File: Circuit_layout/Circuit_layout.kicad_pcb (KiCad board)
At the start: 2 copper layers, 177.8 x 127 mm, 188 parts, among them CON1 AVR-JTAG-10, J1 Spare_Conns, J4 Motor_Ctrl, J5 RJ12, P1 TSV, P2 CONN_02X10, P3 CONN_02X07, Q1 ZVP4525G, Q2 MMBF170, Q3 MMBF170, SW1 SW_PUSH, SW2 TS5A3159-Q1, SW3 JS202011CQN, U1 PDM2-S24-S12, U10 MCP2551-I/SN, U11 TLP293, U12 TLP293, U13 PDQ10-D, U16 LTC3638, U17 MCP6004, U18 TS912, U19 ACPL-C870, U2 MCP6002, U20 ACPL-C870, U21 MCP6001, U22 TS372, U23 TLP293, U24 TLP293, U3 MCP6004, U4 LM95071-Q1, U5 LM7810CT, U6 TS912, U7 AT90CAN128-A, U8 74ACT11030, U9 TLP293, Y1 10MHz

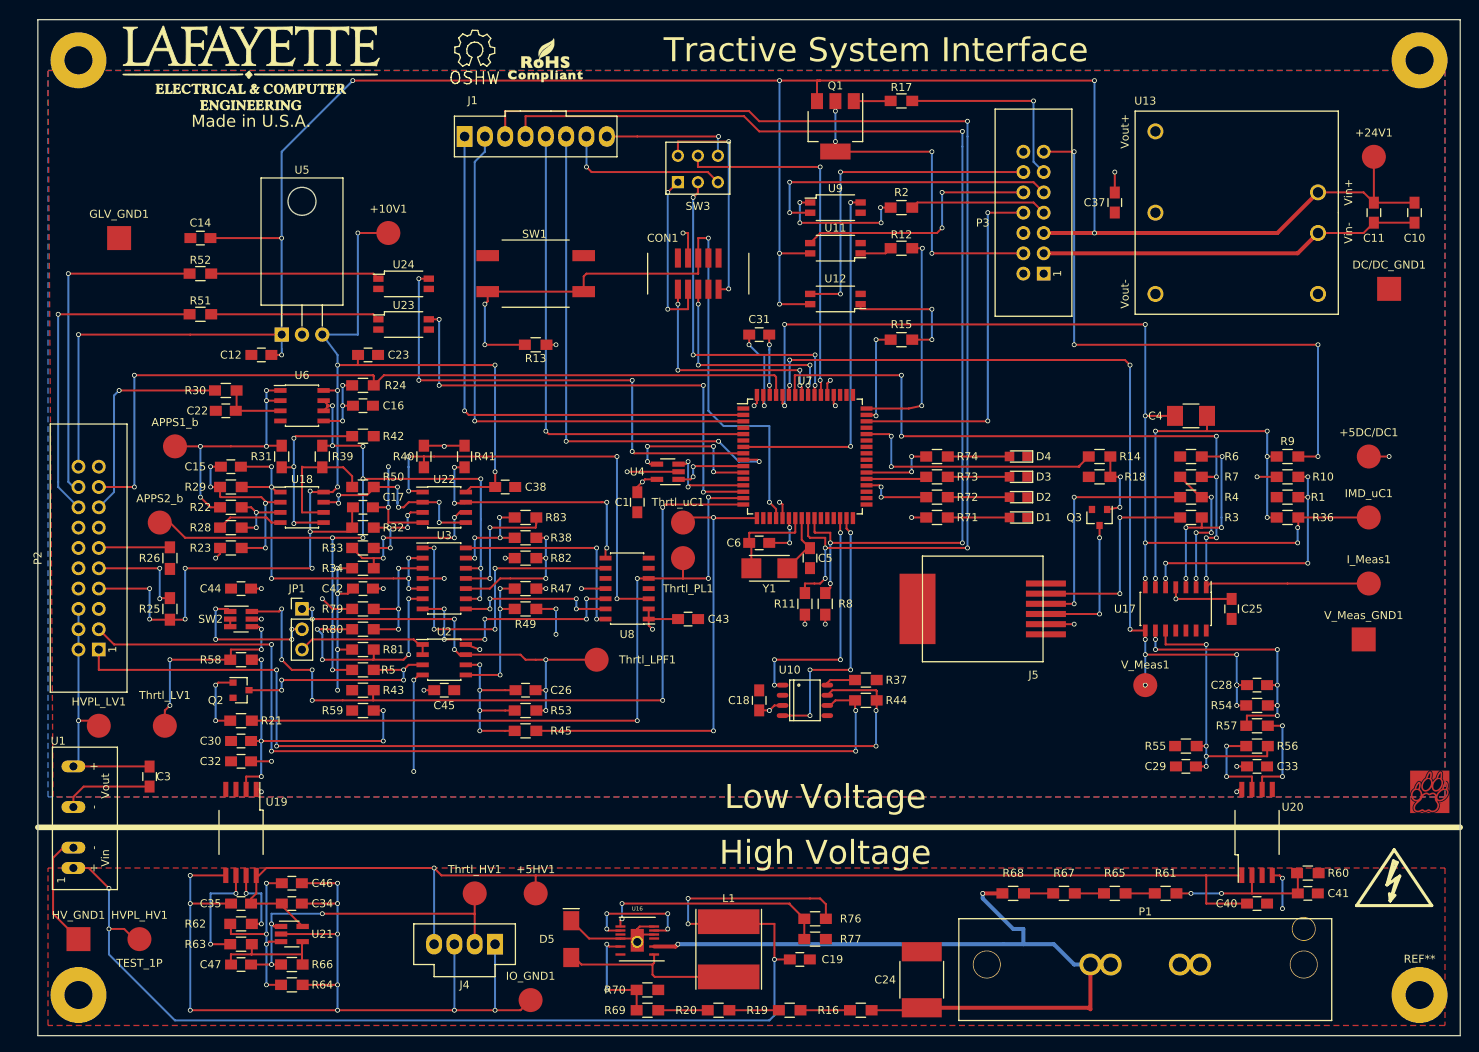
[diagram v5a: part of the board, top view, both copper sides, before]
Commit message: fixed changes proposed by prof. nadovich.
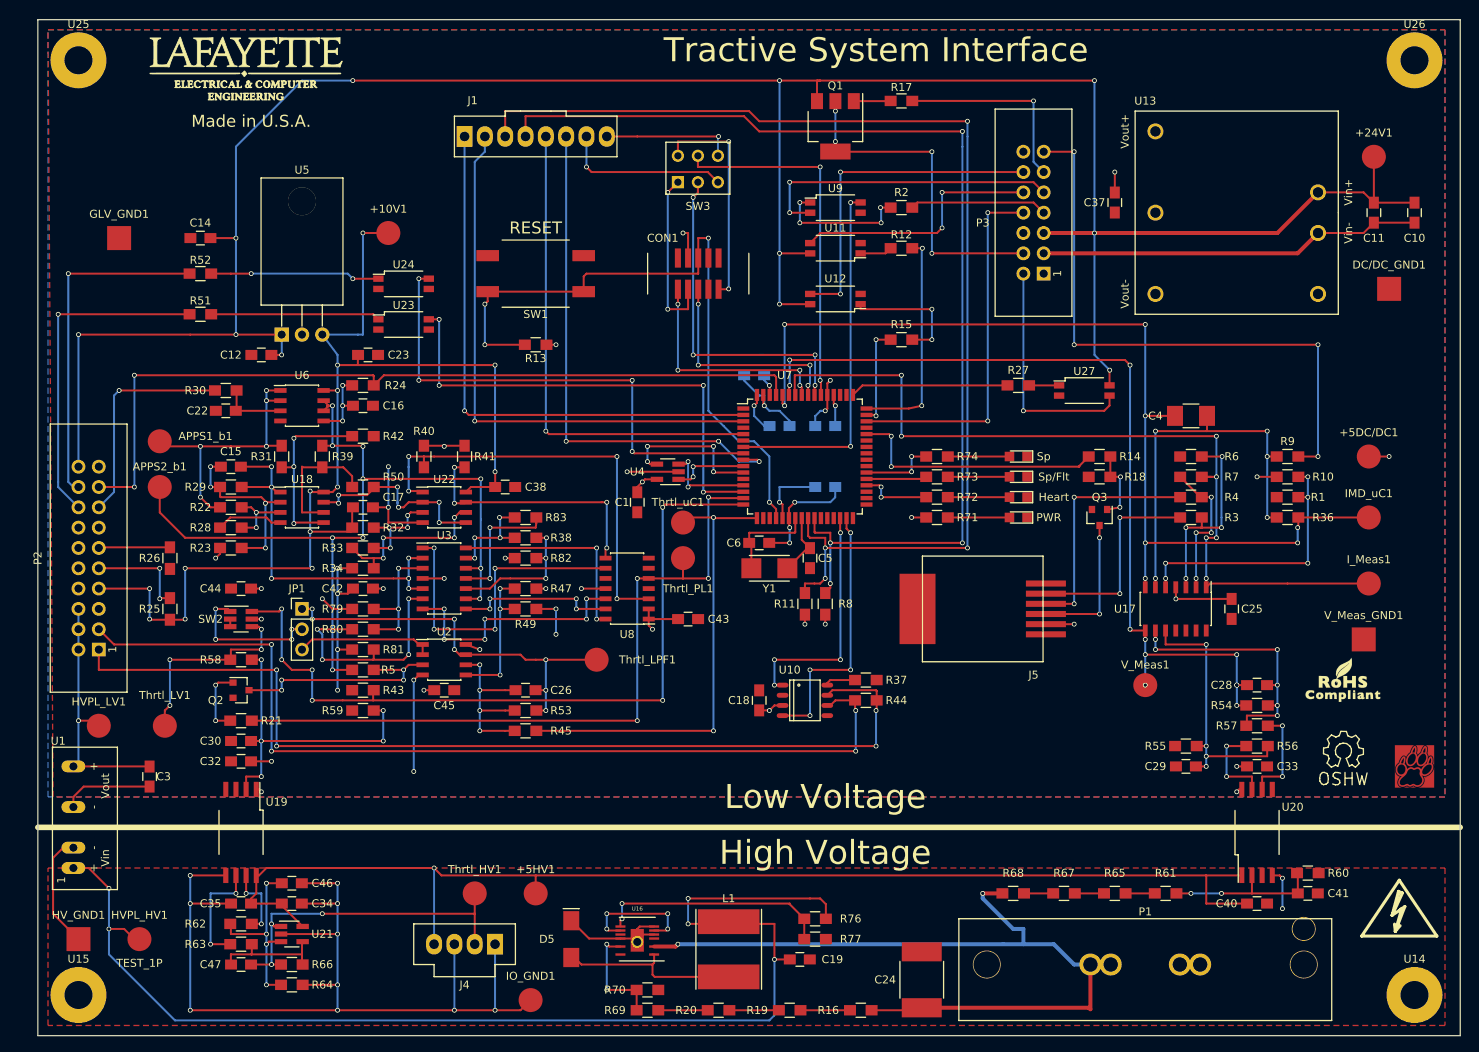
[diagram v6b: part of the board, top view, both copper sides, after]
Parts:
- removed the ? at (35.6, 34.3)
- removed the ? at (203.2, 34.3)
- removed the ? at (35.6, 151.1)
- removed APPS1_b: APPS1_b, Measurement_Points:Measurement_Point_Round-SMD-Pad_Big
- removed APPS2_b: APPS2_b, Measurement_Points:Measurement_Point_Round-SMD-Pad_Big
- removed the G*** at (57.1, 35.6)
- removed the REF** at (203.2, 151.1)
- added APPS1_b1: APPS1_b, Measurement_Points:Measurement_Point_Round-SMD-Pad_Big, F.Cu at (45.7, 81.9)
- added APPS2_b1: APPS2_b, Measurement_Points:Measurement_Point_Round-SMD-Pad_Big, F.Cu at (45.7, 87.6)
- added C2: 0.1u, Capacitors_SMD:C_0805_HandSoldering, B.Cu at (128.9, 80.0)
- added C7: 0.1u, Capacitors_SMD:C_0805_HandSoldering, B.Cu at (123.2, 80.0)
- added C8: 0.1u, Capacitors_SMD:C_0805_HandSoldering, B.Cu at (128.9, 87.6)
- added G***: LOGO, custom_footprints:logo_lafayette_ece_24mmx9mm, F.Cu at (56.5, 35.6)
- added R27: 150, Resistors_SMD:R_0805_HandSoldering, F.Cu at (153.0, 74.9)
- added U14: Mounting_hole, Mounting_Holes:MountingHole_3.5mm_Pad, F.Cu at (202.6, 151.1)
- added U15: Mounting_hole, Mounting_Holes:MountingHole_3.5mm_Pad, F.Cu at (35.6, 151.1)
- added U25: Mounting_hole, Mounting_Holes:MountingHole_3.5mm_Pad, F.Cu at (35.6, 34.3)
- added U26: Mounting_hole, Mounting_Holes:MountingHole_3.5mm_Pad, F.Cu at (202.6, 34.3)
- added U27: TLP293, Housings_SSOP:SOP-4_4.4x2.8mm_Pitch1.27mm, F.Cu at (161.3, 75.6)
- C31: moved to B.Cu
- U5: footprint TO_SOT_Packages_THT:TO-220_Horizontal -> custom_footprints:TO-220_Horizontal_Plated_Hole
- moved REF** 139.5 mm to (193.7, 120.7)
- moved G*** 126.3 mm to (193.7, 111.8)
- moved C31 5.12 mm to (120.0, 73.7)
- moved ? 3.86 mm to (200.7, 141.0)
- moved ? 3.86 mm to (201.3, 141.0)
- moved VAL 3.70 mm to (202.6, 122.6)
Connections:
- P3 pad 2: CH_GND -> CC_LED
- U5 pad 0: (no net) -> CH_GND
- U7 pad 49: Net-(U7-Pad49) -> /Status Lights/CC_LED_CTRL
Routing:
- net CC_LED: track 0.00 -> 29.4 mm, vias 0 -> 1
- net +24V: track 295.2 -> 315.4 mm, vias 10 -> 12
- net /Status Lights/CC_LED_CTRL: track 0.00 -> 19.8 mm
- net CH_GND: track 115.5 -> 129.0 mm, vias 18 -> 19
- net +5V: track 78.8 -> 91.4 mm
- net Net-(C31-Pad1): track 7.57 -> 2.75 mm, vias 2 -> 1
- net Net-(R27-Pad1): track 0.00 -> 3.76 mm
- net /ThrottlePlausibility/APPS2_b: track 102.9 -> 106.6 mm
- net ~RESET_AVR: track 88.3 -> 86.1 mm
- net /ThrottlePlausibility/APPS1_b: track 33.7 -> 35.9 mm
- net (no net): track 0.02 -> 0.65 mm
- net Net-(R52-Pad2): vias 0 -> 2
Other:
- net class Default: clearance 0.254 -> 0.2032
- rule trace_clearance: 0.254 -> 0.2032
- board text added: "Heart"
- board text added: "PWR"
- board text added: "RESET"
- board text added: "Sp"
- board text added: "Sp/Flt"

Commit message: small changes
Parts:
- moved C8 3.86 mm to (125.1, 88.3)
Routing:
- net +5V: track 91.4 -> 86.6 mm
- net CH_GND: track 129.0 -> 128.9 mm, vias 19 -> 20
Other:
- board text added: "Designed by: Jack Plumb and Adam Ness"
- board text removed: "Update U5 to have horizontal footprint"
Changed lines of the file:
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@@
   (general
     (links 413)
-    (no_connects 1)
-    (area 30.404999 29.134999 208.355001 156.285001)
+    (no_connects 0)
+    (area -39.052858 17.47 231.825715 156.905)
     (thickness 1.6)
-    (drawings 18)
-    (tracks 1610)
+    (drawings 21)
+    (tracks 1612)
     (zones 0)
     (modules 193)
@@
     (41 Cmts.User user)
     (42 Eco1.User user)
-    (43 Eco2.User user)
+    (43 Eco2.User user hide)
     (44 Edge.Cuts user)
     (45 Margin user)
@@
     (mod_text_size 1 1)
     (mod_text_width 0.15)
-    (pad_size 3 3)
-    (pad_drill 0)
+    (pad_size 4.5 4.5)
+    (pad_drill 3.5)
     (pad_to_mask_clearance 0.2)
     (aux_axis_origin 0 0)
@@
   )
   (module Capacitors_SMD:C_0805_HandSoldering (layer B.Cu)
-    (at 128.905 87.63)
+    (at 125.095 88.265)
     (descr "Capacitor SMD 0805, hand soldering")
     (tags "capacitor 0805")
@@
     (descr "Mounting Hole 3.5mm")
     (tags "mounting hole 3.5mm")
-    (fp_text reference U14 (at 0 -4.5) (layer F.SilkS)
+    (fp_text reference U14 (at 0 -4.5) (layer F.SilkS) hide
       (effects (font (size 1 1) (thickness 0.15)))
     )
@@
     (descr "Mounting Hole 3.5mm")
     (tags "mounting hole 3.5mm")
-    (fp_text reference U15 (at 0 -4.5) (layer F.SilkS)
+    (fp_text reference U15 (at 0 -4.5) (layer F.SilkS) hide
       (effects (font (size 1 1) (thickness 0.15)))
     )
@@
     (descr "Mounting Hole 3.5mm")
     (tags "mounting hole 3.5mm")
-    (fp_text reference U25 (at 0 -4.5) (layer F.SilkS)
+    (fp_text reference U25 (at 0 -4.5) (layer F.SilkS) hide
       (effects (font (size 1 1) (thickness 0.15)))
     )
@@
     (descr "Mounting Hole 3.5mm")
     (tags "mounting hole 3.5mm")
-    (fp_text reference U26 (at 0 -4.5) (layer F.SilkS)
+    (fp_text reference U26 (at 0 -4.5) (layer F.SilkS) hide
       (effects (font (size 1 1) (thickness 0.15)))
     )
@@
     (fp_line (start 7.79 -19.71) (end -2.71 -19.71) (layer F.CrtYd) (width 0.05))
     (fp_circle (center 2.54 -16.66) (end 4.39 -16.66) (layer F.Fab) (width 0.1))
-    (pad 0 thru_hole circle (at 2.54 -16.66) (size 3.5 3.5) (drill 3.5) (layers *.Cu *.Mask F.SilkS)
+    (pad 0 thru_hole circle (at 2.54 -16.66) (size 4.5 4.5) (drill 3.5) (layers *.Cu *.Mask F.SilkS)
       (net 1 CH_GND))
     (pad 1 thru_hole rect (at 0 0) (size 1.8 1.8) (drill 1) (layers *.Cu *.Mask)
@@
       (xy 0.465667 0.021167)) (layer F.SilkS) (width 0.01))
   )
+  (gr_text "High Voltage" (at 128.905 133.35) (layer B.SilkS)
+    (effects (font (size 3 3) (thickness 0.3)) (justify mirror))
+  )
+  (gr_text "Low Voltage" (at 128.905 126.365) (layer B.SilkS)
+    (effects (font (size 3 3) (thickness 0.3)) (justify mirror))
+  )
+  (gr_line (start 208.28 130.175) (end 30.48 130.175) (angle 90) (layer B.SilkS) (width 0.7))
+  (gr_text "Designed by:\nJack Plumb and Adam Ness" (at 176.53 35.56) (layer F.SilkS)
+    (effects (font (size 2 2) (thickness 0.3)))
+  )
   (gr_text Sp (at 156.21 83.82) (layer F.SilkS)
     (effects (font (size 1 1) (thickness 0.15)))
@@
   )
   (gr_line (start 208.28 130.175) (end 30.48 130.175) (angle 90) (layer F.SilkS) (width 0.7))
-  (gr_text "Tractive System Interface" (at 135.255 33.02) (layer F.SilkS)
+  (gr_text "Tractive System Interface" (at 123.19 33.655) (layer F.SilkS)
     (effects (font (size 3 3) (thickness 0.3)))
   )
@@
     (effects (font (size 1.5 1.5) (thickness 0.3)))
   )
-  (gr_text "Update U5 to have horizontal footprint" (at -16.51 71.12) (layer Dwgs.User)
-    (effects (font (size 1.5 1.5) (thickness 0.3)))
-  )
   (segment (start -19.685 151.13) (end -19.665 151.13) (width 0.25) (layer F.Cu) (net 0))
   (segment (start 121.285 71.12) (end 120.65 71.12) (width 0.25) (layer B.Cu) (net 0))
+  (segment (start 125.095 89.535) (end 125.095 89.515) (width 0.25) (layer B.Cu) (net 1))
+  (segment (start 124.365 90.265) (end 125.095 89.535) (width 0.25) (layer F.Cu) (net 1))
+  (via (at 125.095 89.535) (size 0.6) (drill 0.4) (layers F.Cu B.Cu) (net 1))
+  (segment (start 124.365 91.52) (end 124.365 90.265) (width 0.25) (layer F.Cu) (net 1))
+  (segment (start 125.095 89.515) (end 126.345 88.265) (width 0.25) (layer B.Cu) (net 1))
+  (segment (start 129.54 74.295) (end 129.54 70.485) (width 0.25) (layer B.Cu) (net 1))
+  (segment (start 129.165 74.67) (end 129.54 74.295) (width 0.25) (layer F.Cu) (net 1))
+  (via (at 129.54 74.295) (size 0.6) (drill 0.4) (layers F.Cu B.Cu) (net 1))
+  (segment (start 129.165 76.12) (end 129.165 74.67) (width 0.25) (layer F.Cu) (net 1))
+  (via (at 130.175 69.85) (size 0.6) (drill 0.4) (layers F.Cu B.Cu) (net 1))
+  (segment (start 129.54 70.485) (end 130.175 69.85) (width 0.25) (layer B.Cu) (net 1))
   (segment (start 118.765 73.66) (end 118.765 74.315) (width 0.25) (layer B.Cu) (net 1))
   (segment (start 121.285 76.2) (end 121.285 77.47) (width 0.25) (layer B.Cu) (net 1))
   (segment (start 120.65 76.2) (end 121.285 76.2) (width 0.25) (layer B.Cu) (net 1))
   (segment (start 118.765 74.315) (end 120.65 76.2) (width 0.25) (layer B.Cu) (net 1))
-  (segment (start 125.095 89.535) (end 129.54 89.535) (width 0.25) (layer B.Cu) (net 1))
-  (segment (start 124.365 90.265) (end 125.095 89.535) (width 0.25) (layer F.Cu) (net 1))
-  (via (at 125.095 89.535) (size 0.6) (drill 0.4) (layers F.Cu B.Cu) (net 1))
-  (segment (start 124.365 91.52) (end 124.365 90.265) (width 0.25) (layer F.Cu) (net 1))
-  (segment (start 130.155 88.92) (end 130.155 87.63) (width 0.25) (layer B.Cu) (net 1))
-  (segment (start 129.54 89.535) (end 130.155 88.92) (width 0.25) (layer B.Cu) (net 1))
   (segment (start 127.655 80.01) (end 127.655 78.76) (width 0.25) (layer B.Cu) (net 1))
   (segment (start 129.165 77.845) (end 128.905 78.105) (width 0.25) (layer F.Cu) (net 1))
@@
   (segment (start 123.19 78.105) (end 124.44 79.355) (width 0.25) (layer B.Cu) (net 1))
   (segment (start 121.92 78.105) (end 123.19 78.105) (width 0.25) (layer B.Cu) (net 1))
-  (segment (start 129.165 76.12) (end 129.165 74.67) (width 0.25) (layer F.Cu) (net 1))
-  (via (at 129.54 74.295) (size 0.6) (drill 0.4) (layers F.Cu B.Cu) (net 1))
-  (segment (start 129.165 74.67) (end 129.54 74.295) (width 0.25) (layer F.Cu) (net 1))
   (segment (start 34.925 127.635) (end 34.925 126.365) (width 0.25) (layer F.Cu) (net 1))
   (segment (start 36.215 125.075) (end 44.45 125.075) (width 0.25) (layer F.Cu) (net 1))
@@
   (via (at 121.285 77.47) (size 0.6) (drill 0.4) (layers F.Cu B.Cu) (net 1))
   (segment (start 121.9 94.615) (end 124.46 94.615) (width 0.25) (layer F.Cu) (net 1))
-  (segment (start 124.365 92.615) (end 124.365 91.52) (width 0.25) (layer F.Cu) (net 1))
-  (segment (start 124.46 92.71) (end 124.365 92.615) (width 0.25) (layer F.Cu) (net 1))
-  (via (at 124.46 92.71) (size 0.6) (drill 0.4) (layers F.Cu B.Cu) (net 1))
-  (segment (start 124.46 94.615) (end 124.46 92.71) (width 0.25) (layer B.Cu) (net 1))
   (via (at 124.46 94.615) (size 0.6) (drill 0.4) (layers F.Cu B.Cu) (net 1))
+  (segment (start 124.46 94.615) (end 124.46 92.71) (width 0.25) (layer B.Cu) (net 1))
+  (via (at 124.46 92.71) (size 0.6) (drill 0.4) (layers F.Cu B.Cu) (net 1))
+  (segment (start 124.46 92.71) (end 124.365 92.615) (width 0.25) (layer F.Cu) (net 1))
+  (segment (start 124.365 92.615) (end 124.365 91.52) (width 0.25) (layer F.Cu) (net 1))
   (via (at 67.945 113.03) (size 0.6) (drill 0.4) (layers F.Cu B.Cu) (net 1))
   (segment (start 67.945 107.95) (end 67.945 113.03) (width 0.25) (layer B.Cu) (net 1))
@@
   (segment (start 104.775 83.185) (end 105.01 83.42) (width 0.25) (layer F.Cu) (net 127))
   (via (at 104.775 83.185) (size 0.6) (drill 0.4) (layers F.Cu B.Cu) (net 127))
+  (segment (start 123.19 89.535) (end 123.19 88.92) (width 0.25) (layer B.Cu) (net 128))
+  (segment (start 123.565 89.795) (end 123.19 89.535) (width 0.25) (layer F.Cu) (net 128))
+  (via (at 123.19 89.535) (size 0.6) (drill 0.4) (layers F.Cu B.Cu) (net 128))
+  (segment (start 123.565 91.52) (end 123.565 89.795) (width 0.25) (layer F.Cu) (net 128) (status 10))
+  (segment (start 123.19 88.92) (end 123.845 88.265) (width 0.25) (layer B.Cu) (net 128))
   (segment (start 130.155 80.01) (end 130.155 77.49) (width 0.25) (layer B.Cu) (net 128))
   (segment (start 129.965 77.26) (end 130.175 77.47) (width 0.25) (layer F.Cu) (net 128))
@@
   (segment (start 121.285 80.01) (end 120.015 78.74) (width 0.25) (layer B.Cu) (net 128))
   (segment (start 120.015 78.74) (end 120.015 77.47) (width 0.25) (layer B.Cu) (net 128))
-  (segment (start 123.19 89.535) (end 123.19 87.63) (width 0.25) (layer B.Cu) (net 128))
-  (segment (start 123.565 89.795) (end 123.19 89.535) (width 0.25) (layer F.Cu) (net 128))
-  (via (at 123.19 89.535) (size 0.6) (drill 0.4) (layers F.Cu B.Cu) (net 128))
-  (segment (start 123.565 91.52) (end 123.565 89.795) (width 0.25) (layer F.Cu) (net 128) (status 10))
-  (segment (start 123.19 87.63) (end 127.655 87.63) (width 0.25) (layer B.Cu) (net 128))
   (segment (start 120.365 76.12) (end 120.365 77.12) (width 0.25) (layer F.Cu) (net 128) (status 10))
   (via (at 120.015 77.47) (size 0.6) (drill 0.4) (layers F.Cu B.Cu) (net 128))
